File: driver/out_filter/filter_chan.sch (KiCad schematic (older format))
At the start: 19 parts, among them T201 300:1

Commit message: Revision 0 of out_filter board.  Tweaks to footprints, reducing pad size.  General routing and pours.
filter_chan.sch:
deleted some testpoints, added input connector.

out_filter.sch:
Added output connector, changed ground testpoint footprint.
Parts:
- removed TP204: Out hot, TestPoint:TestPoint_Keystone_5000-5004_Miniature, symbol Connector:TestPoint
- removed TP205: Out com, TestPoint:TestPoint_Keystone_5000-5004_Miniature, symbol Connector:TestPoint
- added J201: Driver in, Connector_Molex:Molex_Mini-Fit_Jr_5566-02A_2x01_P4.20mm_Vertical, symbol Connector_Generic:Conn_01x02
- R207: DK line M.29 -> M.12; Description RES 100 OHM 1% 1/8W 0603 -> RES 0 OHM JUMPER 1/10W 0603; Digikey RNCP0603FTD100RCT-ND -> RMCF0603ZT0R00CT-ND; MPN RNCP0603FTD100R -> RMCF0603ZT0R00
- W201: DK line OF.8 -> (none); Description CURR SENSE XFMR 70A T/H -> Current transformer primary; Digikey 237-1100-ND -> (none); MPN CST206-3A -> (none); Manufacturer Triad Magnetics -> (none)
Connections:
- net IN_COM: now also J201.2 (Pin_2)
- net IN_HOT: now also J201.1 (Pin_1)
- net SNUB_HOT: now reaches C202.1, R202.1
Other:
- note removed: "C_out (Cx01 || Cx05) can have fairly high current, and should be\nlow-loss (polypropylene). On X channel (7.5 kHz, 940 nF) this is 2A @\n50V RMS. More realistic would be 35 VRMS, or 1.5A RMS. Current is\nlower for the other channels. Be careful with substitutions. Having\ntwo caps in parallel allows flexibility in getting the right\ncapacitance for the channels.\n\n\n\n\n\n\n\n"
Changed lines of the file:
@@
 	1    0    0    -1
 $EndComp
-Text HLabel 1350 1750 0    50   Input ~ 0
-IN_HOT
-Text HLabel 1350 3950 0    50   Input ~ 0
-IN_COM
 Text HLabel 7550 1750 2    50   Output ~ 0
 OUT_HOT
@@
 Wire Wire Line
 	3400 2700 3400 1750
-Wire Wire Line
-	1350 3950 1500 3950
 $Comp
 L ilemt_input:CT_primary W201
@@
 F 1 "3 turns" H 5600 3800 50  0000 C CNN
 F 2 "input:CT_jumper" H 5600 3950 50  0001 C CNN
-F 3 "http://catalog.triadmagnetics.com/Asset/CST206-3A.pdf" H 5600 3950 50  0001 C CNN
-F 4 "OF.8" H 5600 3950 50  0001 C CNN "DK line"
-F 5 "CURR SENSE XFMR 70A T/H" H 5600 3950 50  0001 C CNN "Description"
-F 6 "237-1100-ND" H 5600 3950 50  0001 C CNN "Digikey"
-F 7 "CST206-3A" H 5600 3950 50  0001 C CNN "MPN"
-F 8 "Triad Magnetics" H 5600 3950 50  0001 C CNN "Manufacturer"
+F 3 "?" H 5600 3950 50  0001 C CNN
+F 4 "" H 5600 3950 50  0001 C CNN "DK line"
+F 5 "Current transformer primary" H 5600 3950 50  0001 C CNN "Description"
+F 6 "" H 5600 3950 50  0001 C CNN "Digikey"
+F 7 "" H 5600 3950 50  0001 C CNN "MPN"
+F 8 "" H 5600 3950 50  0001 C CNN "Manufacturer"
 	1    5600 3950
 	-1   0    0    1
@@
 	4950 3950 5400 3950
 Connection ~ 4950 3950
-Wire Wire Line
-	5800 3950 5950 3950
 $Comp
 L power:Earth #PWR0202
@@
 	6250 1750 6250 2350
 Connection ~ 6250 1750
-Wire Wire Line
-	6250 1750 6700 1750
 Wire Wire Line
 	6250 2650 6250 2850
@@
 V sense divide by 101
 Wire Wire Line
-	6700 1700 6700 1750
-Connection ~ 6700 1750
-Wire Wire Line
-	6700 1750 7100 1750
-Wire Wire Line
-	5950 3900 5950 3950
-Wire Wire Line
 	1500 1700 1500 1750
 Connection ~ 1500 1750
-Wire Wire Line
-	1500 1750 1350 1750
 Wire Wire Line
 	1500 3900 1500 3950
@@
 Text Notes 1450 2400 0    50   ~ 0
 Operating voltage is currently 35 VRMS\nor lower.  With +/-80VDC bus, 50 VRMS\nis about the max the driver can support, \nbut distortion increases at the high end.
-Text Notes 3700 2050 0    50   ~ 0
-C_out (Cx01 || Cx05) can have fairly high current, and should be\nlow-loss (polypropylene).  On X channel (7.5 kHz, 940 nF) this is 2A @\n50V RMS.  More realistic would be 35 VRMS, or 1.5A RMS.  Current is\nlower for the other channels.  Be careful with substitutions.  Having\ntwo caps in parallel allows flexibility in getting the right\ncapacitance for the channels.\n\n\n\n\n\n\n\n
 $Comp
 L Device:C_Small C205
@@
 Connection ~ 3100 1250
 $Comp
-L Connector:TestPoint TP204
-U 1 1 5FDC4E04
-P 6700 1700
-AR Path="/5FD7C20A/5FDC4E04" Ref="TP204"  Part="1"
-AR Path="/5FD938D7/5FDC4E04" Ref="TP304"  Part="1"
-AR Path="/5FD93D92/5FDC4E04" Ref="TP404"  Part="1"
-F 0 "TP204" H 6700 1970 50  0000 C CNN
-F 1 "Out hot" H 6700 1900 50  0000 C CNN
-F 2 "TestPoint:TestPoint_Keystone_5000-5004_Miniature" H 6900 1700 50  0001 C CNN
-F 3 "http://keyelco.com/userAssets/file/M65p56.pdf" H 6900 1700 50  0001 C CNN
-F 4 "Optional Keystone 5000-5004" H 6700 1700 50  0001 C CNN "Description"
-F 5 "DNP" H 6700 1700 50  0001 C CNN "MPN"
-F 6 "Keystone Electronics" H 6700 1700 50  0001 C CNN "Manufacturer"
-	1    6700 1700
-	1    0    0    -1
-$EndComp
-$Comp
-L Connector:TestPoint TP205
-U 1 1 5FDC560F
-P 5950 3900
-AR Path="/5FD7C20A/5FDC560F" Ref="TP205"  Part="1"
-AR Path="/5FD938D7/5FDC560F" Ref="TP305"  Part="1"
-AR Path="/5FD93D92/5FDC560F" Ref="TP405"  Part="1"
-F 0 "TP205" H 5950 4170 50  0000 C CNN
-F 1 "Out com" H 5950 4100 50  0000 C CNN
-F 2 "TestPoint:TestPoint_Keystone_5000-5004_Miniature" H 6150 3900 50  0001 C CNN
-F 3 "http://keyelco.com/userAssets/file/M65p56.pdf" H 6150 3900 50  0001 C CNN
-F 4 "Optional Keystone 5000-5004" H 5950 3900 50  0001 C CNN "Description"
-F 5 "DNP" H 5950 3900 50  0001 C CNN "MPN"
-F 6 "Keystone Electronics" H 5950 3900 50  0001 C CNN "Manufacturer"
-	1    5950 3900
-	1    0    0    -1
-$EndComp
-$Comp
 L Connector:TestPoint TP201
 U 1 1 5FDC6B44
@@
 F 1 "0" V 6450 3550 50  0000 C CNN
 F 2 "Resistor_SMD:R_0603_1608Metric" V 6590 3540 50  0001 C CNN
-F 3 "https://www.seielect.com/catalog/sei-rncp.pdf" H 6550 3550 50  0001 C CNN
-F 4 "M.29" H 6550 3550 50  0001 C CNN "DK line"
-F 5 "RES 100 OHM 1% 1/8W 0603" H 6550 3550 50  0001 C CNN "Description"
-F 6 "RNCP0603FTD100RCT-ND" H 6550 3550 50  0001 C CNN "Digikey"
-F 7 "RNCP0603FTD100R" H 6550 3550 50  0001 C CNN "MPN"
+F 3 "?" H 6550 3550 50  0001 C CNN
+F 4 "M.12" H 6550 3550 50  0001 C CNN "DK line"
+F 5 "RES 0 OHM JUMPER 1/10W 0603" H 6550 3550 50  0001 C CNN "Description"
+F 6 "RMCF0603ZT0R00CT-ND" H 6550 3550 50  0001 C CNN "Digikey"
+F 7 "RMCF0603ZT0R00" H 6550 3550 50  0001 C CNN "MPN"
 F 8 "Stackpole Electronics Inc" H 6550 3550 50  0001 C CNN "Manufacturer"
 	1    6550 3550
@@
 Wire Wire Line
 	6250 3950 7100 3950
-Connection ~ 5950 3950
-Wire Wire Line
-	5950 3950 6250 3950
 Wire Wire Line
 	7100 3950 7500 3950
@@
 Wire Wire Line
 	6250 3350 6250 3550
+$Comp
+L Connector_Generic:Conn_01x02 J?
+U 1 1 5FE35CC0
+P 950 2750
+AR Path="/5FE35CC0" Ref="J?"  Part="1"
+AR Path="/5FD7C20A/5FE35CC0" Ref="J201"  Part="1"
+AR Path="/5FD938D7/5FE35CC0" Ref="J301"  Part="1"
+AR Path="/5FD93D92/5FE35CC0" Ref="J401"  Part="1"
+F 0 "J201" H 950 2850 50  0000 C CNN
+F 1 "Driver in" H 950 2550 50  0000 C CNN
+F 2 "Connector_Molex:Molex_Mini-Fit_Jr_5566-02A_2x01_P4.20mm_Vertical" H 950 2750 50  0001 C CNN
+F 3 "https://www.molex.com/pdm_docs/ps/PS-5556-001.pdf" H 950 2750 50  0001 C CNN
+F 4 "CONN HEADER VERT 2POS" H 950 2750 50  0001 C CNN "Description"
+F 5 "WM23800-ND" H 950 2750 50  0001 C CNN "Digikey"
+F 6 "0039288020" H 950 2750 50  0001 C CNN "MPN"
+F 7 "Molex" H 950 2750 50  0001 C CNN "Manufacturer"
+F 8 "OF.7" H 950 2750 50  0001 C CNN "DK line"
+	1    950  2750
+	-1   0    0    -1
+$EndComp
+Wire Wire Line
+	1150 2750 1150 1750
+Wire Wire Line
+	1150 1750 1500 1750
+Wire Wire Line
+	1150 2850 1150 3950
+Wire Wire Line
+	1150 3950 1500 3950
+Text Label 1150 2500 0    50   ~ 0
+IN_HOT
+Text Label 1150 3200 0    50   ~ 0
+IN_COM
+Text Label 4950 2950 0    50   ~ 0
+SNUB_HOT
+Wire Wire Line
+	5800 3950 6250 3950
+Wire Wire Line
+	6250 1750 7100 1750
 $EndSCHEMATC

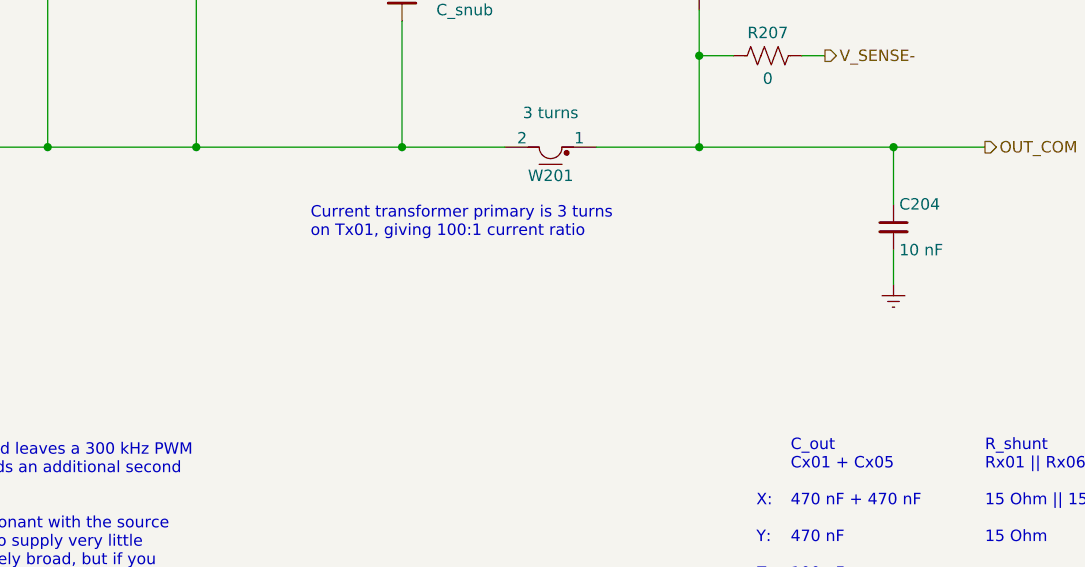
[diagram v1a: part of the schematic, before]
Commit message: Checkpoint before I start ripping the chassis ground components out of input_board.
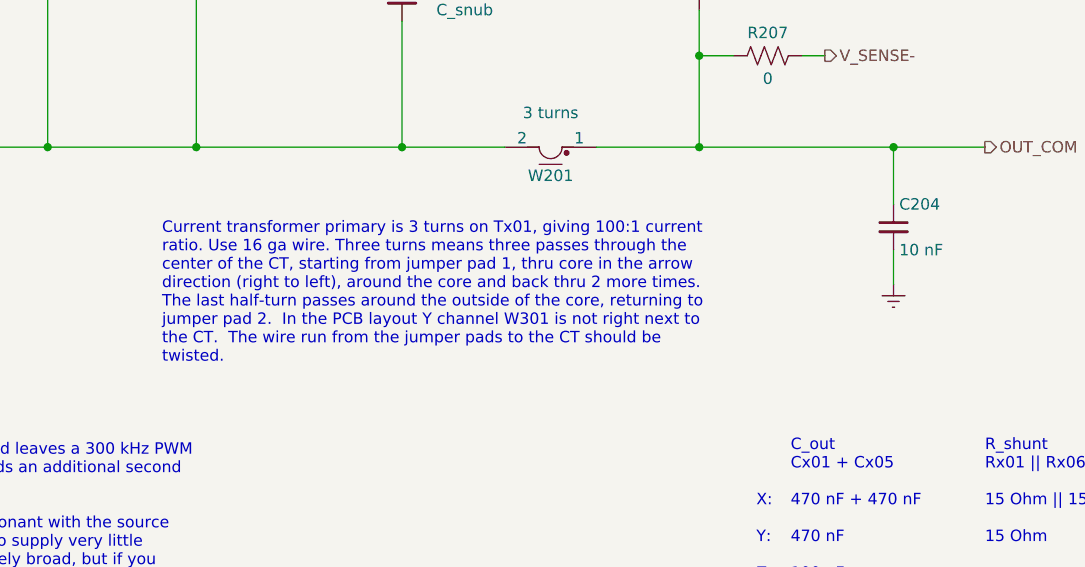
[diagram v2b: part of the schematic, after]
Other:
- note added: "Current transformer primary is 3 turns on Tx01, giving 100:1 current\nratio. Use 16 ga wire. Three turns means three passes through the\ncenter of the CT, starting from jumper pad 1, thru core in the arrow\ndirection (right to left), around the core and back thru 2 more times.\nThe last half-turn passes around the outside of the core, returning to\njumper pad 2. In the PCB layout Y channel W301 i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"
- note removed: "Current transformer primary is 3 turns \non Tx01, giving 100:1 current ratio"
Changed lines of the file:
@@
 	1    0    0    -1
 $EndComp
-Text Notes 4550 4350 0    50   ~ 0
-Current transformer primary is 3 turns \non Tx01, giving 100:1 current ratio
+Text Notes 3900 4900 0    50   ~ 0
+Current transformer primary is 3 turns on Tx01, giving 100:1 current\nratio. Use 16 ga wire. Three turns means three passes through the\ncenter of the CT, starting from jumper pad 1, thru core in the arrow\ndirection (right to left), around the core and back thru 2 more times.\nThe last half-turn passes around the outside of the core, returning to\njumper pad 2.  In the PCB layout Y channel W301 is not right next to\nthe CT.  The wire run from the jumper pads to the CT should be\ntwisted.\n
 $Comp
 L Device:R_US R207

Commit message: Documentation
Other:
- note added: "Current transformer primary is 3 turns on Tx01, giving 100:1 current\nratio. With Rx05 = 5.1 Ohm this gives 51 mV/A at the current sense\noutput, or 0.816 V/A after 16x gain on the input card. The ADC full\nscale is 5V, so the peak current is 6.1A.\n\nUse 16 ga wire. Three turns means three passes through the\ncenter of the CT, starting from jumper pad 1, thru core in the arrow\ndirection (right 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"
- note removed: "Current transformer primary is 3 turns on Tx01, giving 100:1 current\nratio. Use 16 ga wire. Three turns means three passes through the\ncenter of the CT, starting from jumper pad 1, thru core in the arrow\ndirection (right to left), around the core and back thru 2 more times.\nThe last half-turn passes around the outside of the core, returning to\njumper pad 2. In the PCB layout Y channel W301 i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"
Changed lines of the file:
@@
 Text Notes 7100 6850 0    50   ~ 0
 Output filter and feedback sense for one source axis
-Text Notes 6650 5850 0    50   ~ 0
+Text Notes 6650 6150 0    50   ~ 0
 C_out\nCx01 + Cx05\n\n470 nF + 470 nF\n\n470 nF\n\n100 nF\n
-Text Notes 7500 5850 0    50   ~ 0
+Text Notes 7500 6150 0    50   ~ 0
 R_shunt\nRx01 || Rx06\n\n15 Ohm || 15 Ohm\n\n15 Ohm\n\nopen\n
-Text Notes 8400 5850 0    50   ~ 0
+Text Notes 8400 6150 0    50   ~ 0
 C_snub\nCx02\n\nopen\n\nopen\n\n100 nF\n
-Text Notes 8800 5850 0    50   ~ 0
+Text Notes 8800 6150 0    50   ~ 0
 R_snub\nRx02\n\nopen\n\nopen\n\n47 Ohm
-Text Notes 9250 5850 0    50   ~ 0
+Text Notes 9250 6150 0    50   ~ 0
 Parallel \nresonance\n\n9 kHz\n\n10.9 kHz\n\n12.8 kHz\n
-Text Notes 9800 5850 0    50   ~ 0
+Text Notes 9800 6150 0    50   ~ 0
 Series\nresonance\n\n25 kHz\n\n32 kHz\n\n46 kHz\n
-Text Notes 1300 7400 0    50   ~ 0
+Text Notes 1250 7700 0    50   ~ 0
 The 33 uH/470 nF output filter on the IRAUDAMP7 board leaves a 300 kHz PWM\nripple which can be several volts.  This output filter adds an additional second\norder section Lx01/Cx01 to reduce the ripple.\n\nAnother feature is that if C_out + 470 nF is parallel resonant with the source\ncoil at the high carrier frequency, then the driver has to supply very little\ncurrent for the high carrier.  The resonance is moderately broad, but if you\nhave to drive at a different frequency then it's better to go lower, because\nabove the resonance the input current becomes larger than the load current,\nwhereas below the two simply converge.\n\nWe add additional RC snubbers to dampen the series resonance of Lx01 + 33 uH.\nChannels have either Rx01 or Rx02/Cx02 snubbers, but not both.  The "Zobel\nnetwork" snubber on the IRAUDAMP7 is disconnected by removing the capacitor.\n\nSee simetrix/out_filter.sxsch and notebook.txt on 21-23 Jan 16.\n\nDamping the resonance may be a good practice in general, but in particular, this\nresonance for the 7.5 kHz carrier is very near annoying second harmonic\ndistortion products.  Even without those, the noise floor rises in a hump near\nthe resonance (above what it would be without the filter).  For the X channel,\nC101 places the parallel resonance at 8.5 kHz, a bit above the carrier, but\nmaintains considerable current reduction while shifting the series resonance up\nin frequency (above the second harmonic).\n\nPossibly this damping, or even the second filter stage itself, is not entirely\nnecessary.\n
 Text Notes 6600 3250 0    50   ~ 0
@@
 Wire Wire Line
 	4050 3950 4950 3950
-Text Notes 6500 5850 0    50   ~ 0
+Text Notes 6500 6150 0    50   ~ 0
 X:\n\nY:\n\nZ:
-Text Notes 10350 5850 0    50   ~ 0
+Text Notes 10350 6150 0    50   ~ 0
 Carrier freq\n\n7.5 kHz\n\n10.5 kHz\n\n13.5 kHz\n
 $Comp
@@
 	1    0    0    -1
 $EndComp
-Text Notes 3900 4900 0    50   ~ 0
-Current transformer primary is 3 turns on Tx01, giving 100:1 current\nratio. Use 16 ga wire. Three turns means three passes through the\ncenter of the CT, starting from jumper pad 1, thru core in the arrow\ndirection (right to left), around the core and back thru 2 more times.\nThe last half-turn passes around the outside of the core, returning to\njumper pad 2.  In the PCB layout Y channel W301 is not right next to\nthe CT.  The wire run from the jumper pads to the CT should be\ntwisted.\n
+Text Notes 3850 5250 0    50   ~ 0
+Current transformer primary is 3 turns on Tx01, giving 100:1 current\nratio.  With Rx05 = 5.1 Ohm this gives 51 mV/A at the current sense\noutput, or 0.816 V/A after 16x gain on the input card.  The ADC full\nscale is 5V, so the peak current is 6.1A.\n\nUse 16 ga wire. Three turns means three passes through the\ncenter of the CT, starting from jumper pad 1, thru core in the arrow\ndirection (right to left), around the core and back thru 2 more times.\nThe last half-turn passes around the outside of the core, returning to\njumper pad 2.  In the PCB layout Y channel W301 is not right next to\nthe CT.  The wire run from the jumper pads to the CT should be\ntwisted.\n
 $Comp
 L Device:R_US R207
